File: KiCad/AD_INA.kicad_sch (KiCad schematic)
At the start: 0 parts

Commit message: ADD AC623 and INA126 Test Circuitry
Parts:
- added D3, D5: BLU, symbol Device:LED
- added D4, D6: WHT, symbol Device:LED
- added R1, R2: 510, symbol Device:R_Small
- added U2: AD623/INA126, Package_DIP:DIP-8_W7.62mm_Socket, symbol Amplifier_Instrumentation:AD623
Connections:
- new net: D3.2 (A), D4.2 (A), R1.2
- new net: D5.2 (A), D6.2 (A), R2.1
- new net: R2.2, U2.6
- new net REF: D3.1 (K), D4.1 (K), D5.1 (K), D6.1 (K), U2.5 (Ref)
- new net VS+: U2.7 (Vs+)
- new net VS-: U2.4 (Vs-)
- new net Wave: R1.1, U2.3 (+)
- no-connect marks 0 -> 4

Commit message: updated footprint to be all THT, battery holder still not there
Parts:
- D3, D5: footprint (none) -> Diode_THT:D_5W_P5.08mm_Vertical_KathodeUp
- D4, D6: footprint (none) -> Diode_THT:D_5W_P5.08mm_Vertical_AnodeUp
- R1, R2: footprint (none) -> Resistor_THT:R_Axial_DIN0204_L3.6mm_D1.6mm_P2.54mm_Vertical
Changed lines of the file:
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@@
 			)
 		)
-		(property "Footprint" ""
+		(property "Footprint" "Diode_THT:D_5W_P5.08mm_Vertical_KathodeUp"
 			(at 64.77 58.42 0)
 			(effects
@@
 			)
 		)
-		(property "Footprint" ""
+		(property "Footprint" "Resistor_THT:R_Axial_DIN0204_L3.6mm_D1.6mm_P2.54mm_Vertical"
 			(at 58.42 62.23 0)
 			(effects
@@
 			)
 		)
-		(property "Footprint" ""
+		(property "Footprint" "Diode_THT:D_5W_P5.08mm_Vertical_AnodeUp"
 			(at 64.77 88.9 0)
 			(effects
@@
 			)
 		)
-		(property "Footprint" ""
+		(property "Footprint" "Diode_THT:D_5W_P5.08mm_Vertical_KathodeUp"
 			(at 64.77 81.28 0)
 			(effects
@@
 			)
 		)
-		(property "Footprint" ""
+		(property "Footprint" "Diode_THT:D_5W_P5.08mm_Vertical_AnodeUp"
 			(at 64.77 66.04 0)
 			(effects
@@
 			)
 		)
-		(property "Footprint" ""
+		(property "Footprint" "Resistor_THT:R_Axial_DIN0204_L3.6mm_D1.6mm_P2.54mm_Vertical"
 			(at 55.88 85.09 0)
 			(effects

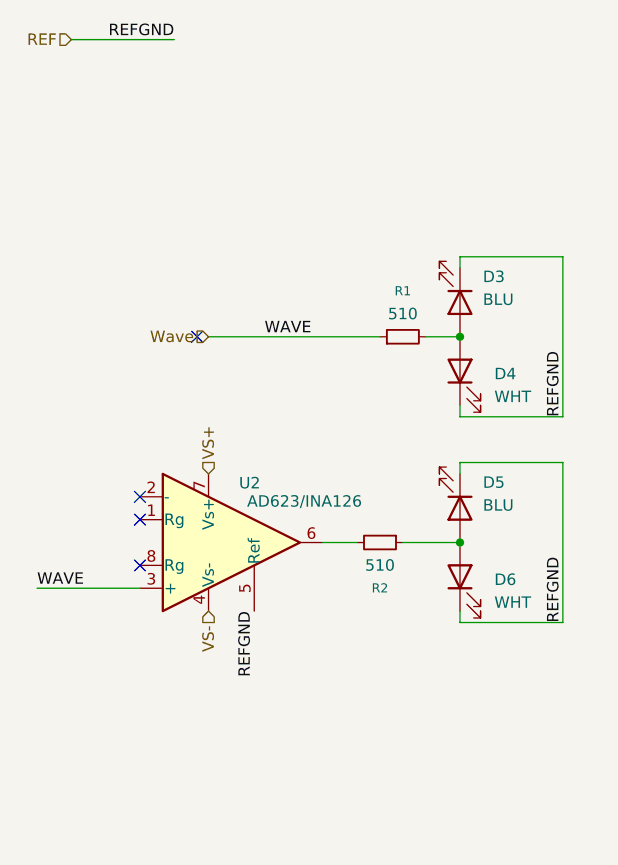
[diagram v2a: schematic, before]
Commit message: Some TP -> Headers, added footprints, fixed battery footprint, started layout of board.
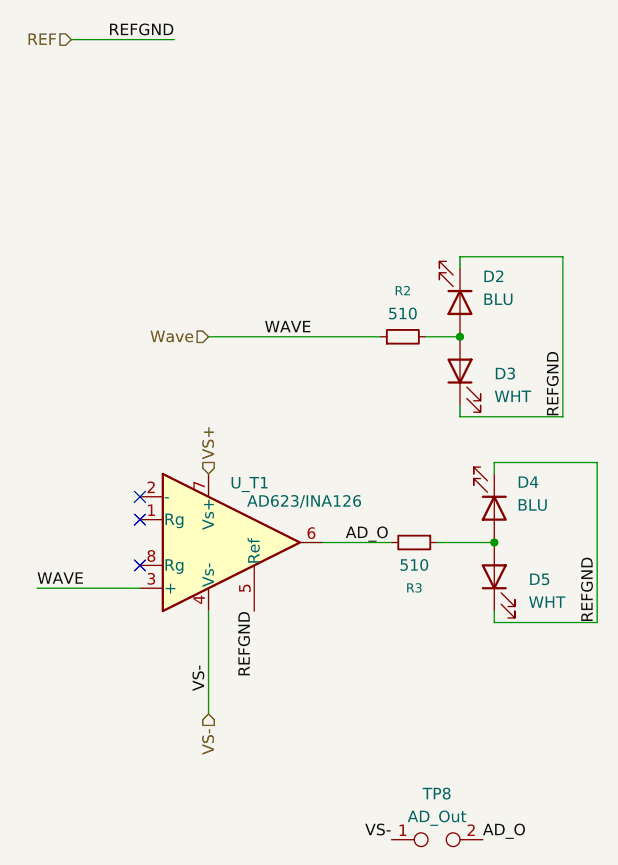
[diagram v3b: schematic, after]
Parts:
- added TP8: AD_Out, Connector_PinSocket_2.54mm:PinSocket_1x02_P2.54mm_Vertical, symbol Connector:TestPoint_2Pole
- renumbered D3 to D2, D4 to D3, D5 to D4, D6 to D5, R1 to R2, R2 to R3, U2 to U_T1
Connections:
- net VS-: now also TP8.1
- net AD_O: now reaches R3.2, U_T1.6
- net AD_O: now also TP8.2
- no-connect marks 4 -> 3
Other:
- moved on the sheet: D4, D5, R3

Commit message: Made the board :D
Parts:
- D2, D4: footprint Diode_THT:D_5W_P5.08mm_Vertical_KathodeUp -> LED_THT:LED_D5.0mm
- D3, D5: footprint Diode_THT:D_5W_P5.08mm_Vertical_AnodeUp -> LED_THT:LED_D5.0mm
- R2, R3: footprint Resistor_THT:R_Axial_DIN0204_L3.6mm_D1.6mm_P2.54mm_Vertical -> Resistor_THT:R_Axial_DIN0207_L6.3mm_D2.5mm_P7.62mm_Horizontal
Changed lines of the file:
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@@
 			)
 		)
-		(property "Footprint" "Diode_THT:D_5W_P5.08mm_Vertical_KathodeUp"
+		(property "Footprint" "LED_THT:LED_D5.0mm"
 			(at 64.77 58.42 0)
 			(effects
@@
 			)
 		)
-		(property "Footprint" "Resistor_THT:R_Axial_DIN0204_L3.6mm_D1.6mm_P2.54mm_Vertical"
+		(property "Footprint" "Resistor_THT:R_Axial_DIN0207_L6.3mm_D2.5mm_P7.62mm_Horizontal"
 			(at 58.42 62.23 0)
 			(effects
@@
 			)
 		)
-		(property "Footprint" "Diode_THT:D_5W_P5.08mm_Vertical_AnodeUp"
+		(property "Footprint" "LED_THT:LED_D5.0mm"
 			(at 68.58 88.9 0)
 			(effects
@@
 			)
 		)
-		(property "Footprint" "Diode_THT:D_5W_P5.08mm_Vertical_KathodeUp"
+		(property "Footprint" "LED_THT:LED_D5.0mm"
 			(at 68.58 81.28 0)
 			(effects
@@
 			)
 		)
-		(property "Footprint" "Diode_THT:D_5W_P5.08mm_Vertical_AnodeUp"
+		(property "Footprint" "LED_THT:LED_D5.0mm"
 			(at 64.77 66.04 0)
 			(effects
@@
 			)
 		)
-		(property "Footprint" "Resistor_THT:R_Axial_DIN0204_L3.6mm_D1.6mm_P2.54mm_Vertical"
+		(property "Footprint" "Resistor_THT:R_Axial_DIN0207_L6.3mm_D2.5mm_P7.62mm_Horizontal"
 			(at 59.69 85.09 0)
 			(effects

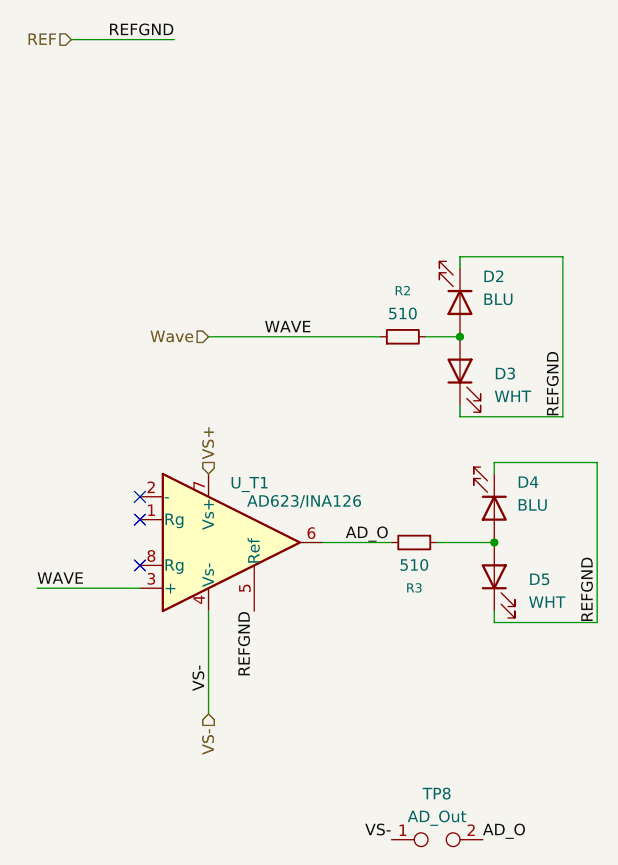
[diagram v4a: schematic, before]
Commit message: Added milling machine files / updated schematic+pcb annotations /  updated footprints
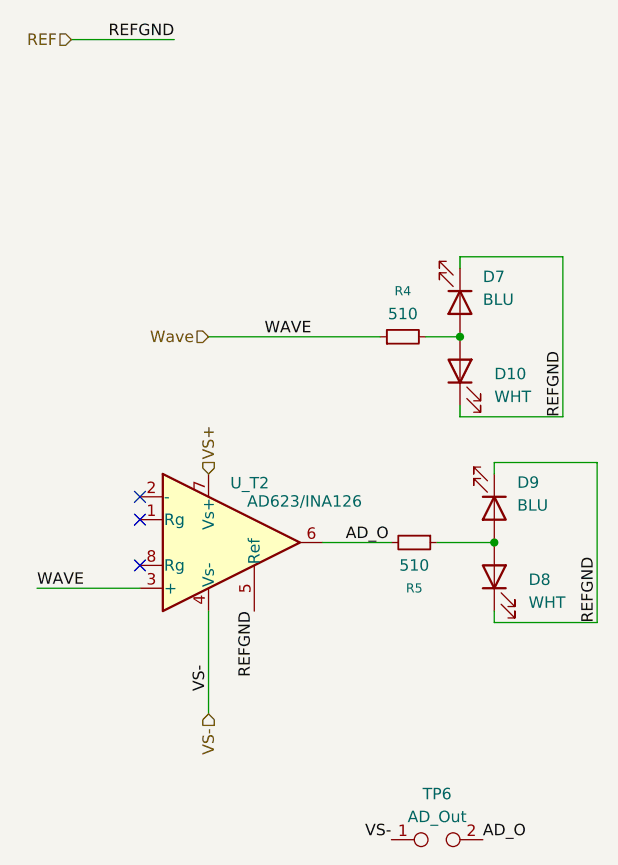
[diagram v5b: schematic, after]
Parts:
- renumbered D3 to D10, D2 to D7, D5 to D8, D4 to D9, R2 to R4, R3 to R5, TP8 to TP6, U_T1 to U_T2
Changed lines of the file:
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@@
 		(dnp no)
 		(fields_autoplaced yes)
-		(property "Reference" "D2"
+		(property "Reference" "D7"
 			(at 67.31 55.5624 90)
 			(effects
@@
 			(project "ChipTester_354"
 				(path "/57b9e980-cd8f-44e4-af61-2cbd5bb30325/2c721cfb-c552-4509-ae86-4c8bd0be2d45"
-					(reference "D2")
+					(reference "D7")
 					(unit 1)
 				)
@@
 		(dnp no)
 		(fields_autoplaced yes)
-		(property "Reference" "R2"
+		(property "Reference" "R4"
 			(at 58.42 57.15 90)
 			(effects
@@
 			(project ""
 				(path "/57b9e980-cd8f-44e4-af61-2cbd5bb30325/2c721cfb-c552-4509-ae86-4c8bd0be2d45"
-					(reference "R2")
+					(reference "R4")
 					(unit 1)
 				)
@@
 		(dnp no)
 		(fields_autoplaced yes)
-		(property "Reference" "D5"
+		(property "Reference" "D8"
 			(at 72.39 89.2174 90)
 			(effects
@@
 			(project "ChipTester_354"
 				(path "/57b9e980-cd8f-44e4-af61-2cbd5bb30325/2c721cfb-c552-4509-ae86-4c8bd0be2d45"
-					(reference "D5")
+					(reference "D8")
 					(unit 1)
 				)
@@
 		(dnp no)
 		(fields_autoplaced yes)
-		(property "Reference" "TP8"
+		(property "Reference" "TP6"
 			(at 62.23 113.03 0)
 			(effects
@@
 			(project "ChipTester_354"
 				(path "/57b9e980-cd8f-44e4-af61-2cbd5bb30325/2c721cfb-c552-4509-ae86-4c8bd0be2d45"
-					(reference "TP8")
+					(reference "TP6")
 					(unit 1)
 				)
@@
 		(dnp no)
 		(fields_autoplaced yes)
-		(property "Reference" "D4"
+		(property "Reference" "D9"
 			(at 71.12 78.4224 90)
 			(effects
@@
 			(project "ChipTester_354"
 				(path "/57b9e980-cd8f-44e4-af61-2cbd5bb30325/2c721cfb-c552-4509-ae86-4c8bd0be2d45"
-					(reference "D4")
+					(reference "D9")
 					(unit 1)
 				)
@@
 		(dnp no)
 		(fields_autoplaced yes)
-		(property "Reference" "D3"
+		(property "Reference" "D10"
 			(at 68.58 66.3574 90)
 			(effects
@@
 			(project "ChipTester_354"
 				(path "/57b9e980-cd8f-44e4-af61-2cbd5bb30325/2c721cfb-c552-4509-ae86-4c8bd0be2d45"
-					(reference "D3")
+					(reference "D10")
 					(unit 1)
 				)
@@
 		(on_board yes)
 		(dnp no)
-		(property "Reference" "R3"
+		(property "Reference" "R5"
 			(at 59.69 90.17 90)
 			(effects
@@
 			(project "ChipTester_354"
 				(path "/57b9e980-cd8f-44e4-af61-2cbd5bb30325/2c721cfb-c552-4509-ae86-4c8bd0be2d45"
-					(reference "R3")
+					(reference "R5")
 					(unit 1)
 				)
@@
 		(on_board yes)
 		(dnp no)
-		(property "Reference" "U_T1"
+		(property "Reference" "U_T2"
 			(at 41.402 78.486 0)
 			(effects
@@
 			(project ""
 				(path "/57b9e980-cd8f-44e4-af61-2cbd5bb30325/2c721cfb-c552-4509-ae86-4c8bd0be2d45"
-					(reference "U_T1")
-					(unit 1)
-				)
+					(reference "U_T2")
+					(unit 1)
+				)
